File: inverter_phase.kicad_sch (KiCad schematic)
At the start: 34 parts, among them Q501 BSC072N08NS5, Q502 BSC072N08NS5, U501 IR2171S, U502 INA180B2

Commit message: feat: component placement, again
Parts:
- removed U502: INA180B2, Package_TO_SOT_SMD:SOT-23-5, symbol Amplifier_Current:INA180A2
- added U702: INA180B2, Package_TO_SOT_SMD:SOT-23-5, symbol Amplifier_Current:INA180B2
- C207: footprint Capacitor_SMD:C_0402_1005Metric_Pad0.74x0.62mm_HandSolder -> Capacitor_SMD:C_0805_2012Metric_Pad1.18x1.45mm_HandSolder
- C224: footprint Capacitor_SMD:C_0603_1608Metric_Pad1.08x0.95mm_HandSolder -> Capacitor_SMD:C_0805_2012Metric_Pad1.18x1.45mm_HandSolder
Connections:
- net +3.3VA: now also U702.5 (V+)
- net GND: now also U702.2 (GND), U702.3 (-)
- net PH_CIN+: now also U702.1 (+)
- net PH_CURR: now also U702.4
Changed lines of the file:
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@@
       (effects (font (size 1.27 1.27)) (justify left))
     )
-    (property "Footprint" "Capacitor_SMD:C_0402_1005Metric_Pad0.74x0.62mm_HandSolder" (at 257.175 86.995 0)
+    (property "Footprint" "Capacitor_SMD:C_0805_2012Metric_Pad1.18x1.45mm_HandSolder" (at 257.175 86.995 0)
       (effects (font (size 1.27 1.27)) hide)
     )
@@
       (effects (font (size 1.27 1.27)) (justify left))
     )
-    (property "Footprint" "Capacitor_SMD:C_0603_1608Metric_Pad1.08x0.95mm_HandSolder" (at 88.9 64.77 0)
+    (property "Footprint" "Capacitor_SMD:C_0805_2012Metric_Pad1.18x1.45mm_HandSolder" (at 88.9 64.77 0)
       (effects (font (size 1.27 1.27)) hide)
     )
@@
     )
   )
-  (symbol (lib_id "Device:C_Small") (at 102.235 64.77 180) (unit 1)
-    (in_bom yes) (on_board yes) (dnp no)
-    (property "Reference" "C502" (at 104.775 63.5 0)
-      (effects (font (size 1.27 1.27)) (justify right))
-    )
-    (property "Value" "100n 50V" (at 104.775 65.405 0)
-      (effects (font (size 1.27 1.27)) (justify right))
-    )
-    (property "Footprint" "Capacitor_SMD:C_0402_1005Metric_Pad0.74x0.62mm_HandSolder" (at 102.235 64.77 0)
-      (effects (font (size 1.27 1.27)) hide)
-    )
-    (property "Datasheet" "~" (at 102.235 64.77 0)
-      (effects (font (size 1.27 1.27)) hide)
-    )
-    (pin "1")
-    (pin "2")
-    (instances
-      (project "ESC_R1"
-        (path "/9dea2e18-5867-4ed4-a12d-7ee109225de0/a82201a8-9dca-4a1d-828e-2de3fb3c1adb"
-          (reference "C502") (unit 1)
-        )
-        (path "/9dea2e18-5867-4ed4-a12d-7ee109225de0/fe2fcbfe-ce2b-4fee-9243-f26c3dcbcd78"
-          (reference "C604") (unit 1)
-        )
-        (path "/9dea2e18-5867-4ed4-a12d-7ee109225de0/4eb0e494-3187-44db-9d3d-24d2fbf5dea7"
-          (reference "C704") (unit 1)
-        )
-      )
-    )
-  )
-  (symbol (lib_id "Device:C_Small") (at 107.95 139.065 180) (unit 1)
-    (in_bom yes) (on_board yes) (dnp no)
-    (property "Reference" "C509" (at 110.49 138.43 0)
-      (effects (font (size 1.27 1.27)) (justify right))
-    )
-    (property "Value" "10n" (at 110.49 140.335 0)
-      (effects (font (size 1.27 1.27)) (justify right))
-    )
-    (property "Footprint" "Capacitor_SMD:C_0603_1608Metric_Pad1.08x0.95mm_HandSolder" (at 107.95 139.065 0)
-      (effects (font (size 1.27 1.27)) hide)
-    )
-    (property "Datasheet" "~" (at 107.95 139.065 0)
-      (effects (font (size 1.27 1.27)) hide)
-    )
-    (pin "1")
-    (pin "2")
-    (instances
-      (project "ESC_R1"
-        (path "/9dea2e18-5867-4ed4-a12d-7ee109225de0/a82201a8-9dca-4a1d-828e-2de3fb3c1adb"
-          (reference "C509") (unit 1)
-        )
-        (path "/9dea2e18-5867-4ed4-a12d-7ee109225de0/fe2fcbfe-ce2b-4fee-9243-f26c3dcbcd78"
-          (reference "C609") (unit 1)
-        )
-        (path "/9dea2e18-5867-4ed4-a12d-7ee109225de0/4eb0e494-3187-44db-9d3d-24d2fbf5dea7"
-          (reference "C709") (unit 1)
-        )
-      )
-    )
-  )
-  (symbol (lib_id "Amplifier_Current:INA180A2") (at 207.645 138.43 0) (mirror y) (unit 1)
-    (in_bom yes) (on_board yes) (dnp no)
-    (property "Reference" "U502" (at 213.995 146.05 0)
-      (effects (font (size 1.27 1.27)))
-    )
-    (property "Value" "INA180B2" (at 203.835 146.05 0)
-      (effects (font (size 1.27 1.27)))
-    )
-    (property "Footprint" "Package_TO_SOT_SMD:SOT-23-5" (at 206.375 137.16 0)
-      (effects (font (size 1.27 1.27)) hide)
-    )
-    (property "Datasheet" "http://www.ti.com/lit/ds/symlink/ina180.pdf" (at 203.835 134.62 0)
-      (effects (font (size 1.27 1.27)) hide)
-    )
-    (property "Link" "https://www.digikey.de/en/products/detail/texas-instruments/INA180B2IDBVR/8105877" (at 207.645 138.43 0)
+  (symbol (lib_id "Amplifier_Current:INA180B2") (at 210.185 138.43 0) (mirror y) (unit 1)
+    (in_bom yes) (on_board yes) (dnp no)
+    (property "Reference" "U702" (at 213.36 145.415 0)
+      (effects (font (size 1.27 1.27)))
+    )
+    (property "Value" "INA180B2" (at 203.835 145.415 0)
+      (effects (font (size 1.27 1.27)))
+    )
+    (property "Footprint" "Package_TO_SOT_SMD:SOT-23-5" (at 210.185 138.43 0)
+      (effects (font (size 1.27 1.27)) hide)
+    )
+    (property "Datasheet" "" (at 210.185 138.43 0)
+      (effects (font (size 1.27 1.27)) hide)
+    )
+    (property "Link" "https://www.digikey.de/en/products/detail/texas-instruments/INA180B2IDBVR/8105877" (at 210.185 138.43 0)
       (effects (font (size 1.27 1.27)) hide)
     )
@@
     (instances
       (project "ESC_R1"
+        (path "/9dea2e18-5867-4ed4-a12d-7ee109225de0/4eb0e494-3187-44db-9d3d-24d2fbf5dea7"
+          (reference "U702") (unit 1)
+        )
         (path "/9dea2e18-5867-4ed4-a12d-7ee109225de0/a82201a8-9dca-4a1d-828e-2de3fb3c1adb"
           (reference "U502") (unit 1)
@@
           (reference "U602") (unit 1)
         )
-        (path "/9dea2e18-5867-4ed4-a12d-7ee109225de0/4eb0e494-3187-44db-9d3d-24d2fbf5dea7"
-          (reference "U702") (unit 1)
-        )
-      )
+      )
+    )
+  )
+  (symbol (lib_id "Device:C_Small") (at 102.235 64.77 180) (unit 1)
+    (in_bom yes) (on_board yes) (dnp no)
+    (property "Reference" "C502" (at 104.775 63.5 0)
+      (effects (font (size 1.27 1.27)) (justify right))
+    )
+    (property "Value" "100n 50V" (at 104.775 65.405 0)
+      (effects (font (size 1.27 1.27)) (justify right))
+    )
+    (property "Footprint" "Capacitor_SMD:C_0402_1005Metric_Pad0.74x0.62mm_HandSolder" (at 102.235 64.77 0)
+      (effects (font (size 1.27 1.27)) hide)
+    )
+    (property "Datasheet" "~" (at 102.235 64.77 0)
+      (effects (font (size 1.27 1.27)) hide)
+    )
+    (pin "1")
+    (pin "2")
+    (instances
+      (project "ESC_R1"
+        (path "/9dea2e18-5867-4ed4-a12d-7ee109225de0/a82201a8-9dca-4a1d-828e-2de3fb3c1adb"
+          (reference "C502") (unit 1)
+        )
+        (path "/9dea2e18-5867-4ed4-a12d-7ee109225de0/fe2fcbfe-ce2b-4fee-9243-f26c3dcbcd78"
+          (reference "C604") (unit 1)
+        )
+        (path "/9dea2e18-5867-4ed4-a12d-7ee109225de0/4eb0e494-3187-44db-9d3d-24d2fbf5dea7"
+          (reference "C704") (unit 1)
+        )
+      )
+    )
+  )
+  (symbol (lib_id "Device:C_Small") (at 107.95 139.065 180) (unit 1)
+    (in_bom yes) (on_board yes) (dnp no)
+    (property "Reference" "C509" (at 110.49 138.43 0)
+      (effects (font (size 1.27 1.27)) (justify right))
+    )
+    (property "Value" "10n" (at 110.49 140.335 0)
+      (effects (font (size 1.27 1.27)) (justify right))
+    )
+    (property "Footprint" "Capacitor_SMD:C_0603_1608Metric_Pad1.08x0.95mm_HandSolder" (at 107.95 139.065 0)
+      (effects (font (size 1.27 1.27)) hide)
+    )
+    (property "Datasheet" "~" (at 107.95 139.065 0)
+      (effects (font (size 1.27 1.27)) hide)
+    )
+    (pin "1")
+    (pin "2")
+    (instances
+      (project "ESC_R1"
+        (path "/9dea2e18-5867-4ed4-a12d-7ee109225de0/a82201a8-9dca-4a1d-828e-2de3fb3c1adb"
+          (reference "C509") (unit 1)
+        )
+        (path "/9dea2e18-5867-4ed4-a12d-7ee109225de0/fe2fcbfe-ce2b-4fee-9243-f26c3dcbcd78"
+          (reference "C609") (unit 1)
+        )
+        (path "/9dea2e18-5867-4ed4-a12d-7ee109225de0/4eb0e494-3187-44db-9d3d-24d2fbf5dea7"
+          (reference "C709") (unit 1)
+        )
+      )

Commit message: chore: project update
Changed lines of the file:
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@@
     (effects (font (face "Avenir Medium") (size 0.8 0.8) (color 0 0 0 1)) (justify left top))
-  )
-  (text_box "LAYOUT NOTE\nRoute shunt traces as differential pair"
-    (at 240.665 140.97 0) (size 20.955 5.08)
-    (stroke (width 0.5) (type solid) (color 0 0 194 1))
-    (fill (type color) (color 255 255 255 1))
-    (effects (font (face "Avenir Medium") (size 0.8 0.8) (color 0 0 194 1)) (justify left top))
   )
   (text_box "DESIGN NOTE\nf_{c}=160kHz"

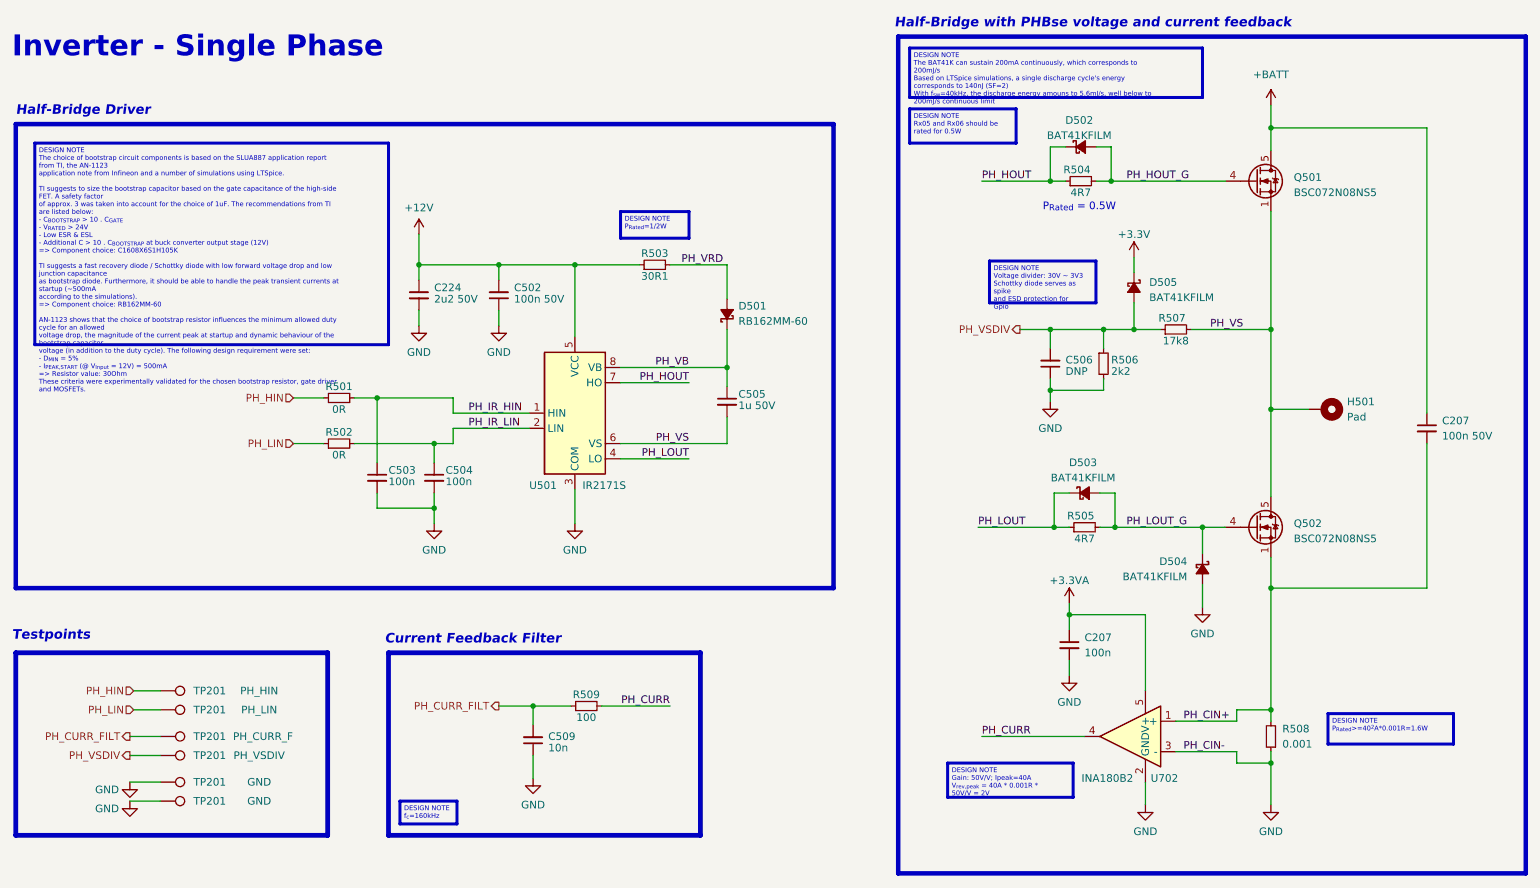
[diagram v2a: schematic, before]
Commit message: feat: finished inverter placement and routing
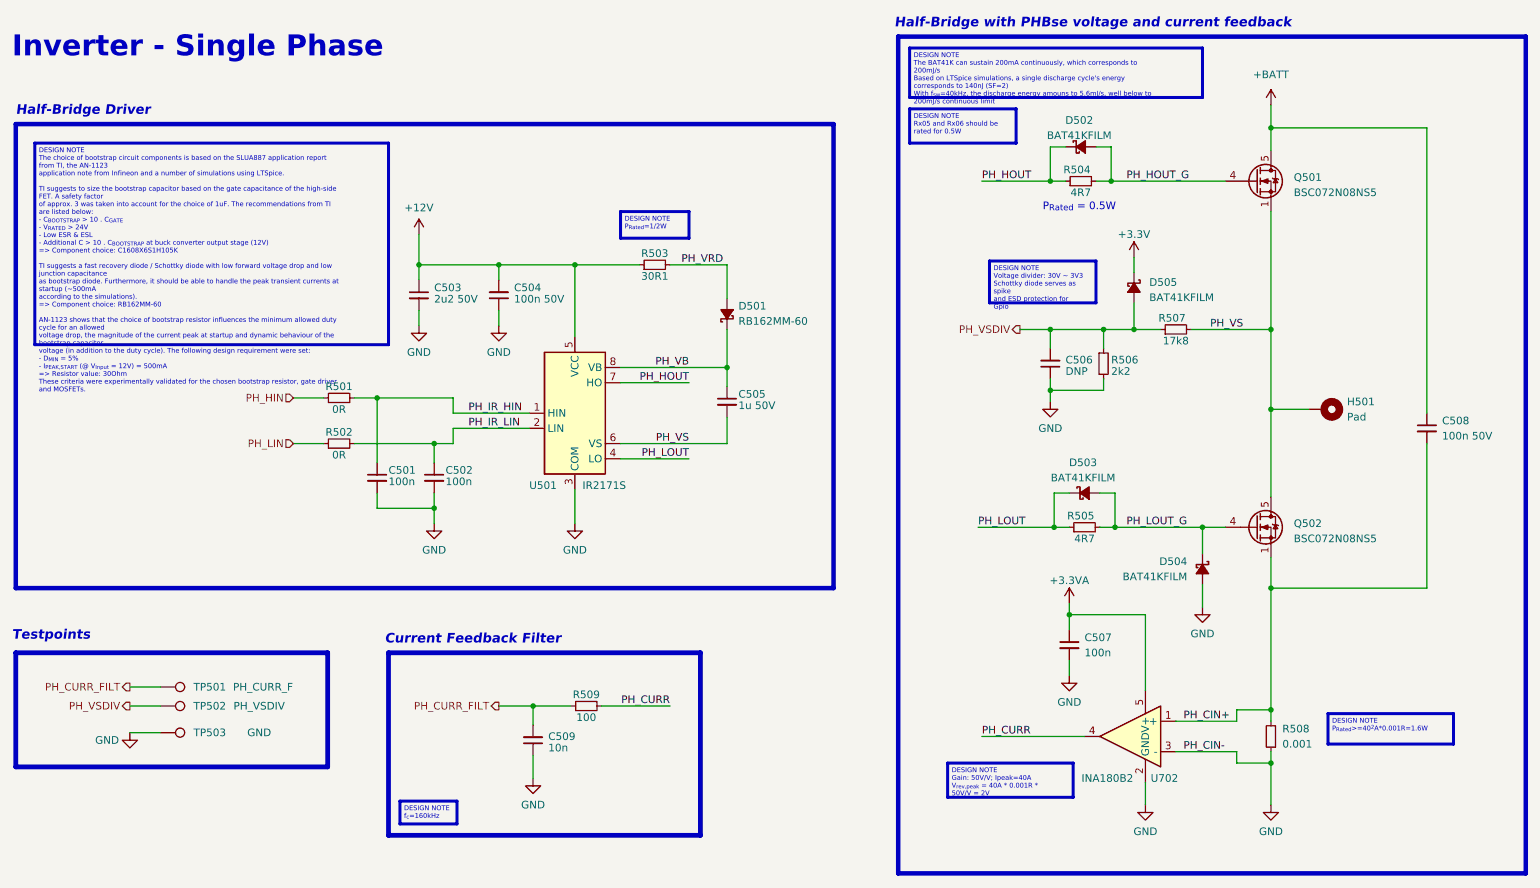
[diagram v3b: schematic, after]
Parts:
- removed TP201: PH_LIN, TestPoint:TestPoint_Pad_D1.5mm, symbol Connector:TestPoint
- removed TP201: PH_HIN, TestPoint:TestPoint_Pad_D1.5mm, symbol Connector:TestPoint
- removed TP201: GND, TestPoint:TestPoint_Pad_D1.5mm, symbol Connector:TestPoint
- H501: footprint TestPoint:Pad_5.5x5.5mm -> TestPoint:HC_Phase_Pad_6x6
- TP501, TP502, TP503: renamed from TP201; footprint TestPoint:TestPoint_Pad_D1.5mm -> TestPoint:TestPoint_Pad_D1.0mm
- renumbered C503 to C501, C504 to C502, C224 to C503, C502 to C504, C207 to C507, C207 to C508
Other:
- moved on the sheet: TP501, TP502, TP503
